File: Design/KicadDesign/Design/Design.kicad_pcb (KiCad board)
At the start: 2 copper layers, 170.7 x 101 mm, 19 parts, among them J1 Speaker, J2 SourceSupply, J3 Jack 3.5 mm, J4 Conn_01x20_Socket, J5 Conn_01x20_Socket, Q1 IRLZ44N, Q2 IRLZ44N, U1 IR2110

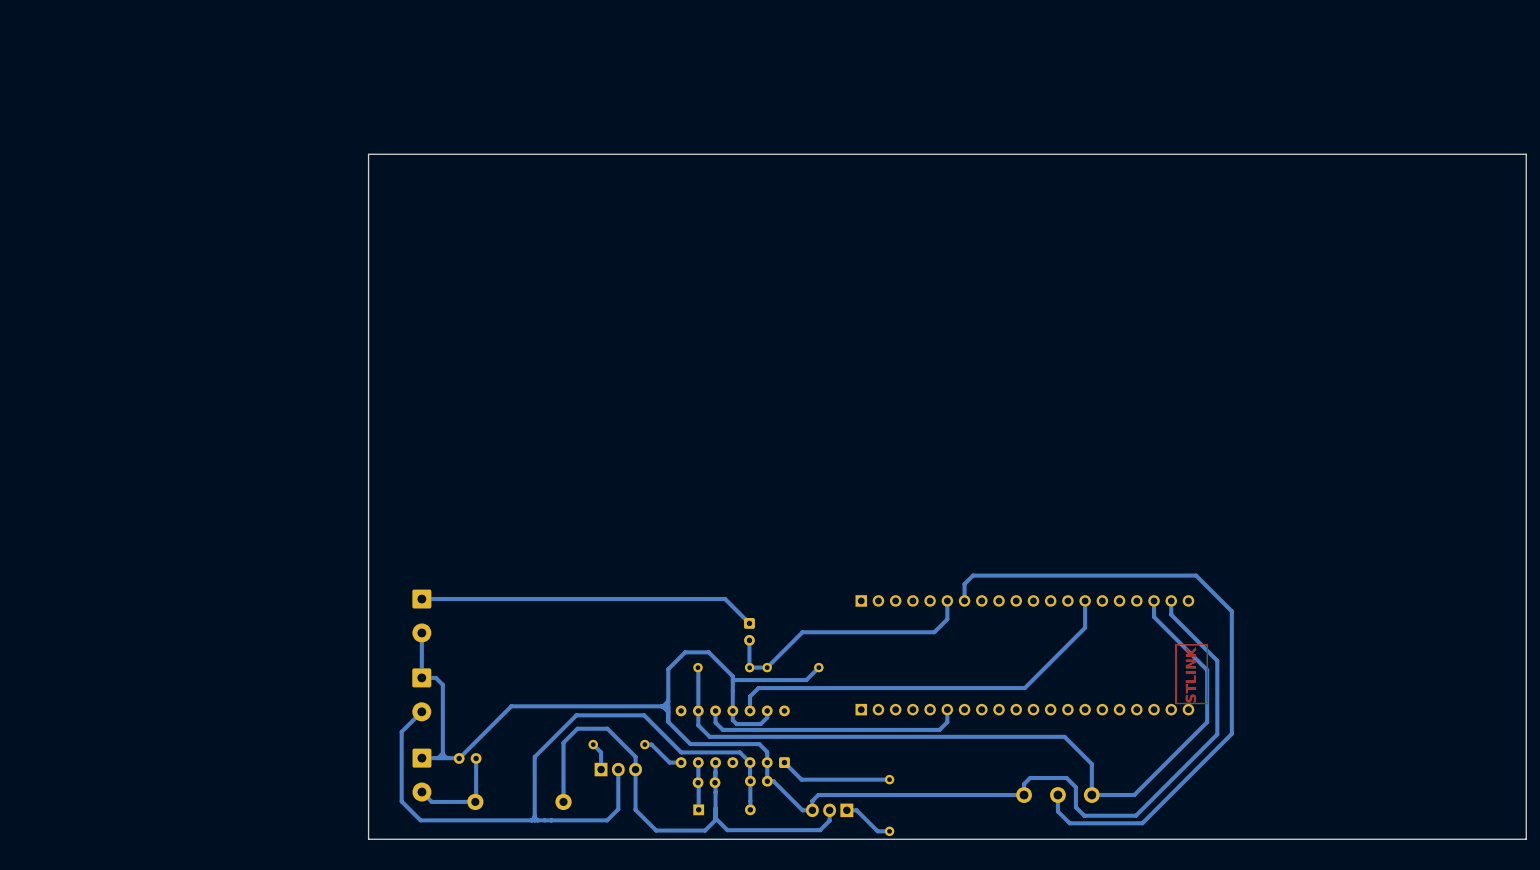
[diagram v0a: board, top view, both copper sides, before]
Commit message: Updated pin B0->B1 A9->A10
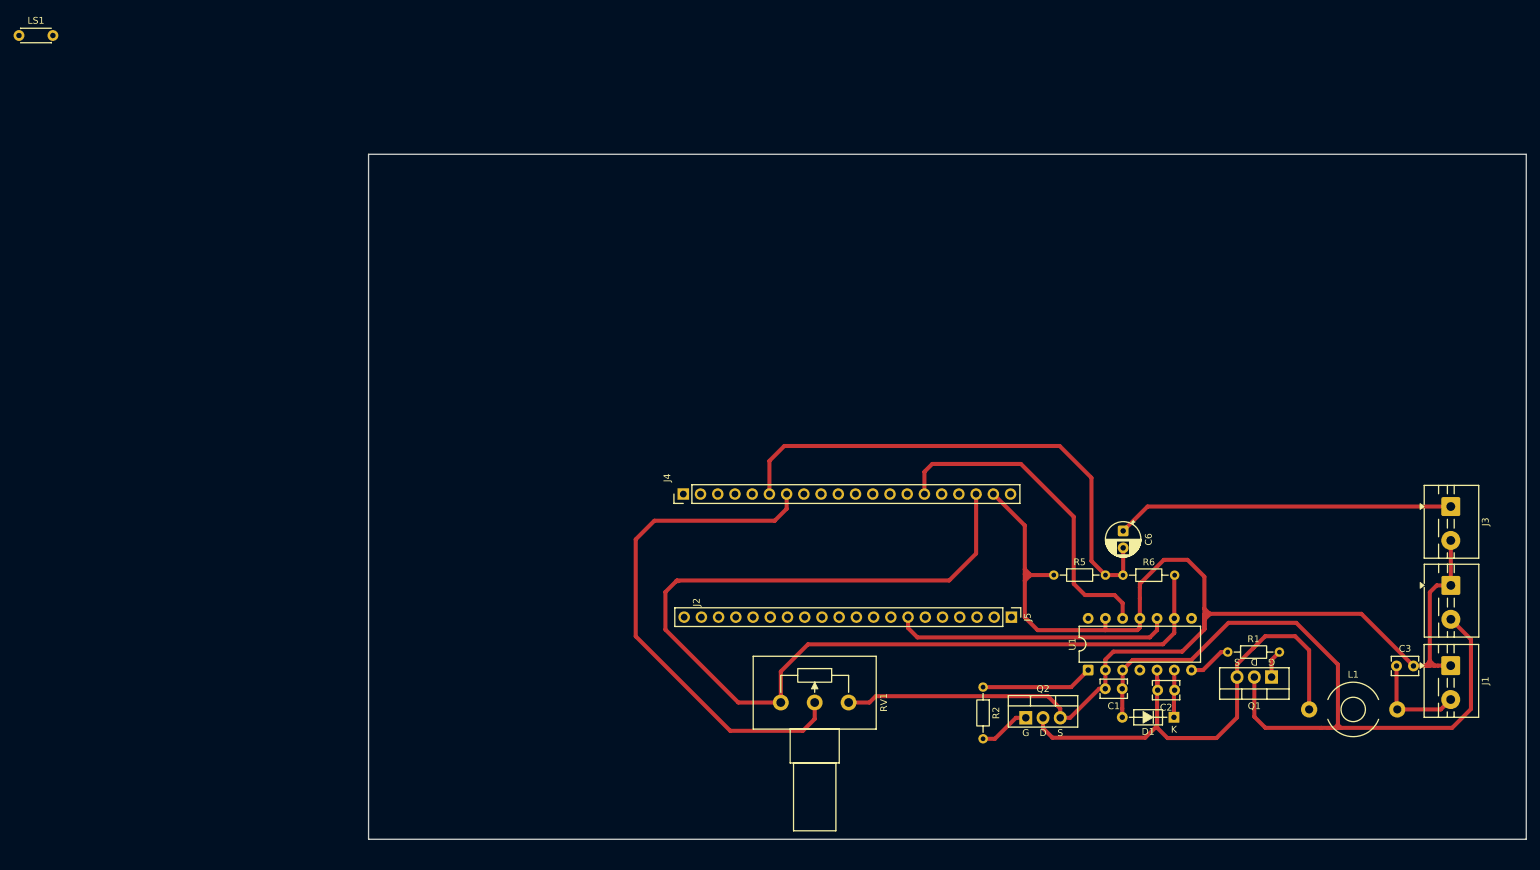
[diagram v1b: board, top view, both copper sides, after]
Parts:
- added LS1: Speaker, Capacitor_THT:C_Disc_D4.3mm_W1.9mm_P5.00mm, F.Cu at (1.07, 1.23)
- C1, C2, C3, C6, D1, J1, J2, J3, J4, J5, L1, Q1, Q2, R1, R2, R5, R6, RV1, U1: moved to F.Cu
- moved J2 152.4 mm to (212.2, 82.3)
- moved J3 152.3 mm to (212.2, 70.7)
- moved J1 152.3 mm to (212.2, 94.1)
- moved C3 136.4 mm to (204.2, 94.2), turned to 0 degrees
- moved L1 110.8 mm to (191.3, 100.6), turned to 0 degrees
- moved Q1 99.8 mm to (185.8, 95.8), turned to 180 degrees
- moved R1 87.0 mm to (179.3, 92.1), turned to 0 degrees
- moved C2 71.6 mm to (171.5, 97.8), turned to 180 degrees
- moved D1 71.4 mm to (171.4, 101.8), turned to 180 degrees
- moved C6 56.8 mm to (163.9, 74.3)
- moved R6 56.7 mm to (163.9, 80.8), turned to 0 degrees
- moved C1 56.5 mm to (163.8, 97.6), turned to 180 degrees
- moved RV1 47.9 mm to (113.4, 99.6)
- moved U1 46.8 mm to (158.7, 94.8)
- moved R5 37.2 mm to (153.7, 80.8), turned to 0 degrees
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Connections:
- J4 pad 14: B0 PWM_N -> B0
- J4 pad 15: unconnected-(J4-Pin_15-Pad15) -> B1 PWM_N
- J4 pad 16: unconnected-(J4-Pin_16-Pad16) -> B2
- J4 pad 17: unconnected-(J4-Pin_17-Pad17) -> B10
- J5 pad 5: unconnected-(J5-Pin_5-Pad5) -> A8
- J5 pad 6: A9 PWM -> A9
- J5 pad 7: unconnected-(J5-Pin_7-Pad7) -> A10 PWM
- U1 pad 10: A9 PWM -> A10 PWM
- U1 pad 12: B0 PWM_N -> B1 PWM_N
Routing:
- net B0 PWM_N: track 59.7 -> 0.00 mm
- net B1 PWM_N: track 0.00 -> 49.5 mm
- net 3.3V: track 116.1 -> 157.8 mm
- net A10 PWM: track 0.00 -> 41.1 mm
- net A9 PWM: track 38.7 -> 0.00 mm
- net A0 ADC1: track 38.9 -> 77.4 mm
- net GND: track 237.5 -> 202.5 mm
- net A1 ADC2: track 96.9 -> 75.9 mm
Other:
- board text removed: "STLINK"

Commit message: Minor fixes on PCB
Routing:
- net GND: track 202.5 -> 199.0 mm
- net B1 PWM_N: track 49.5 -> 51.4 mm

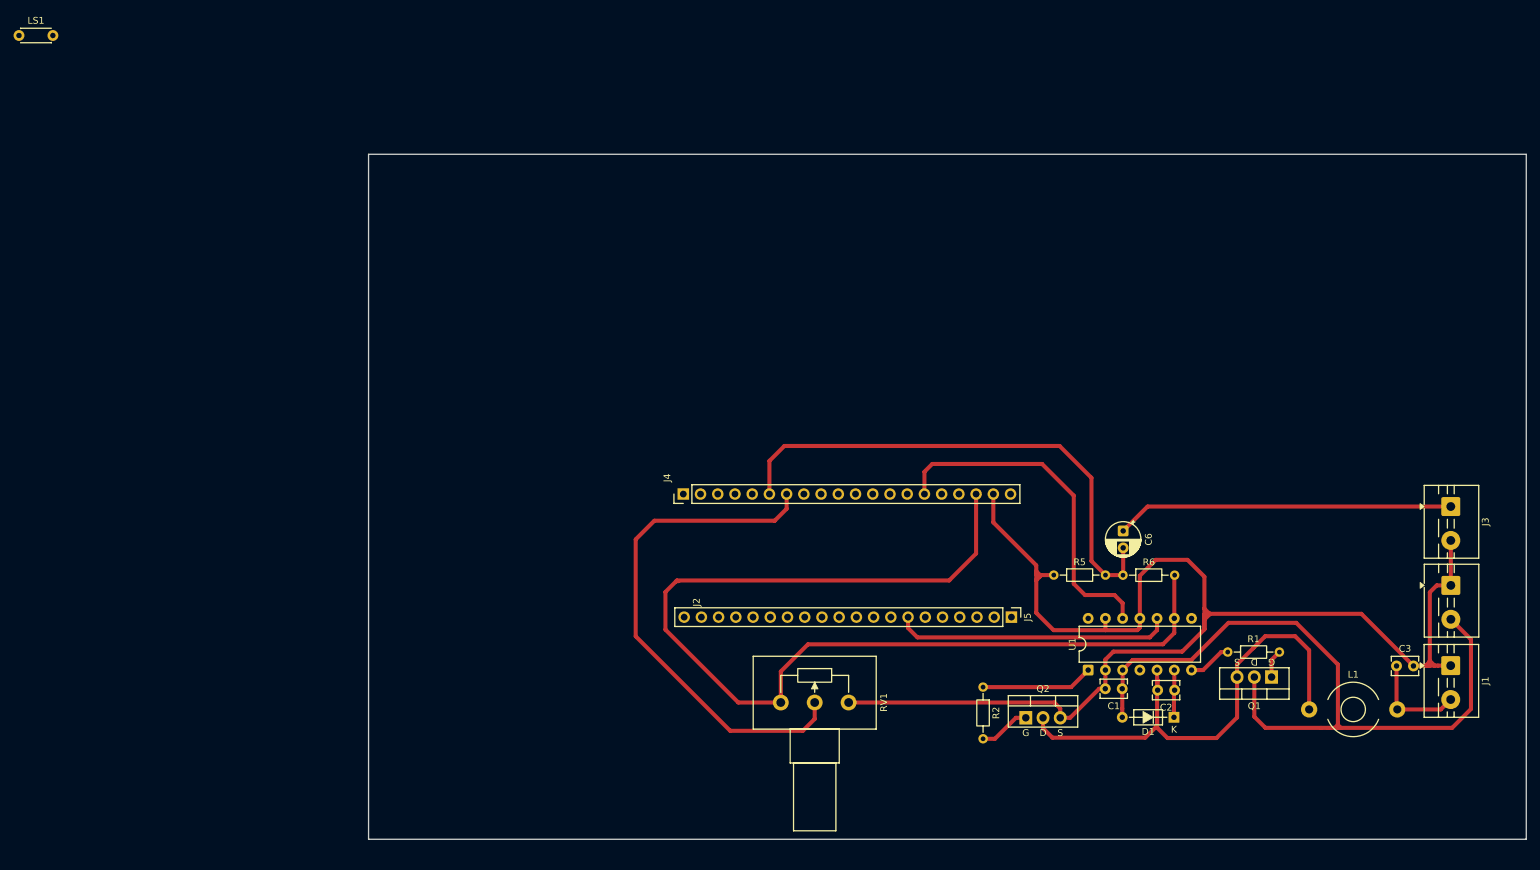
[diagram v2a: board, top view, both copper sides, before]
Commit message: Added Report and Updated Caps on Design
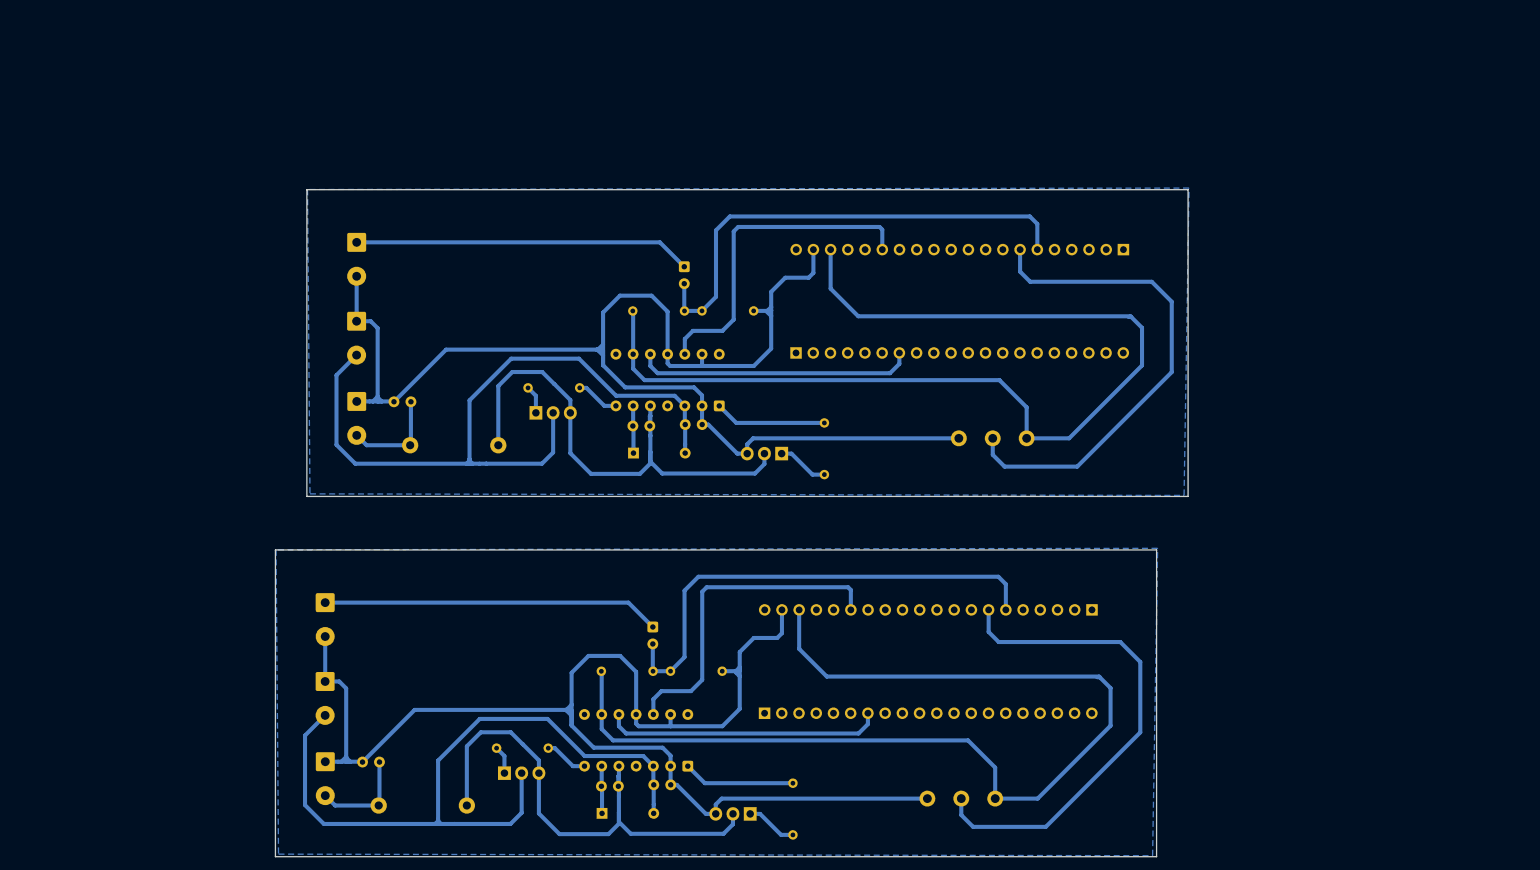
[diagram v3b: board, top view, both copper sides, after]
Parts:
- removed LS1: Speaker, Capacitor_THT:C_Disc_D4.3mm_W1.9mm_P5.00mm
- added C1: 470n, Capacitor_THT:C_Disc_D3.8mm_W2.6mm_P2.50mm, B.Cu at (99.3, 58.6)
- added C2: 470n, Capacitor_THT:C_Disc_D3.8mm_W2.6mm_P2.50mm, B.Cu at (91.6, 58.8)
- added C3: 470n, Capacitor_THT:C_Disc_D3.8mm_W2.6mm_P2.50mm, B.Cu at (58.9, 55.2)
- added C6: 4.7u, Capacitor_THT:CP_Radial_D5.0mm_P2.50mm, B.Cu at (99.2, 35.3)
- added D1: 1N4148, PCM_Diode_THT_AKL:D_DO-35_SOD27_P7.62mm_Horizontal, B.Cu at (91.7, 62.8)
- added J1: Speaker, TerminalBlock:TerminalBlock_MaiXu_MX126-5.0-02P_1x02_P5.00mm, B.Cu at (50.9, 55.2)
- added J2: SourceSupply, TerminalBlock:TerminalBlock_MaiXu_MX126-5.0-02P_1x02_P5.00mm, B.Cu at (50.9, 43.4)
- added J3: Jack 3.5 mm, TerminalBlock:TerminalBlock_MaiXu_MX126-5.0-02P_1x02_P5.00mm, B.Cu at (50.9, 31.7)
- added J4: Conn_01x20_Socket, Connector_PinHeader_2.54mm:PinHeader_1x20_P2.54mm_Vertical, B.Cu at (163.9, 32.8)
- added J5: Conn_01x20_Socket, Connector_PinHeader_2.54mm:PinHeader_1x20_P2.54mm_Vertical, B.Cu at (115.7, 48.0)
- added L1: L, Inductor_THT:L_Toroid_Horizontal_D7.8mm_P13.00mm_Diameter9-5mm_Amidon-T30, B.Cu at (71.8, 61.6)
- added Q1: IRLZ44N, PCM_Package_TO_SOT_THT_AKL:TO-220-3_Vertical_GDS, B.Cu at (77.3, 56.9)
- added Q2: IRLZ44N, PCM_Package_TO_SOT_THT_AKL:TO-220-3_Vertical_GDS, B.Cu at (113.5, 62.9)
- added R1: 22, Resistor_THT:R_Axial_DIN0204_L3.6mm_D1.6mm_P7.62mm_Horizontal, B.Cu at (83.8, 53.2)
- added R2: 22, Resistor_THT:R_Axial_DIN0204_L3.6mm_D1.6mm_P7.62mm_Horizontal, B.Cu at (119.8, 58.4)
- added R5: 10k, Resistor_THT:R_Axial_DIN0204_L3.6mm_D1.6mm_P7.62mm_Horizontal, B.Cu at (109.4, 41.8)
- added R6: 10k, Resistor_THT:R_Axial_DIN0204_L3.6mm_D1.6mm_P7.62mm_Horizontal, B.Cu at (99.2, 41.9)
- added RV1: 20K, PCM_Potentiometer_THT_AKL:Potentiometer_Alps_RK163_Single_Horizontal, B.Cu at (149.7, 60.6)
- added U1: IR2110, Package_DIP:DIP-14_W7.62mm, B.Cu at (104.3, 55.8)
- C1, C2, C3, C6, D1, J1, J2, J3, J4, J5, L1, Q1, Q2, R1, R2, R5, R6, RV1, U1: moved to B.Cu
- moved J2 166.6 mm to (46.2, 96.5)
- moved J3 166.6 mm to (46.2, 84.9)
- moved J1 166.6 mm to (46.2, 108.3)
- moved C3 150.6 mm to (54.2, 108.4), turned to 180 degrees
- moved L1 125.0 mm to (67.1, 114.8), turned to 180 degrees
- moved Q1 114.0 mm to (72.7, 110.0), turned to 0 degrees
- moved R1 101.2 mm to (79.1, 106.3), turned to 180 degrees
- moved C2 85.7 mm to (87.0, 111.9), turned to 0 degrees
- moved D1 85.5 mm to (87.1, 115.9), turned to 0 degrees
- moved C6 70.8 mm to (94.5, 88.5)
- moved R6 70.7 mm to (94.6, 95.0), turned to 180 degrees
- moved C1 70.5 mm to (94.7, 111.7), turned to 0 degrees
- moved J4 62.6 mm to (159.3, 85.9)
- moved U1 60.7 mm to (99.7, 109.0)
- moved R5 50.9 mm to (104.8, 95.0), turned to 180 degrees
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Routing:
- net GND: track 199.0 -> 396.0 mm
- net 3.3V: track 157.8 -> 309.9 mm
- net 12V: track 109.0 -> 218.1 mm
- net Net-(Q1-S): track 74.6 -> 149.2 mm
- net A1 ADC2: track 75.9 -> 146.3 mm
- net A0 ADC1: track 77.4 -> 143.7 mm
- net Net-(J3-Pin_1): track 49.8 -> 99.6 mm
- net B1 PWM_N: track 51.4 -> 97.9 mm
- net A10 PWM: track 41.1 -> 82.2 mm
- net Net-(U1-LO): track 16.5 -> 33.1 mm
- net Net-(J1-Pin_2): track 14.9 -> 29.9 mm
- net Net-(Q2-G): track 7.58 -> 15.2 mm
- net VB: track 7.02 -> 14.0 mm
- net Net-(U1-HO): track 6.44 -> 12.9 mm
- net Net-(Q1-G): track 4.17 -> 8.33 mm
- added copper zone on B.Cu, net GND
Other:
- board size 170.7 x 101 mm -> 134.6 x 98.4 mm
